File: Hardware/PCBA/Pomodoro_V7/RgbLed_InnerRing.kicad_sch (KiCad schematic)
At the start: 8 parts

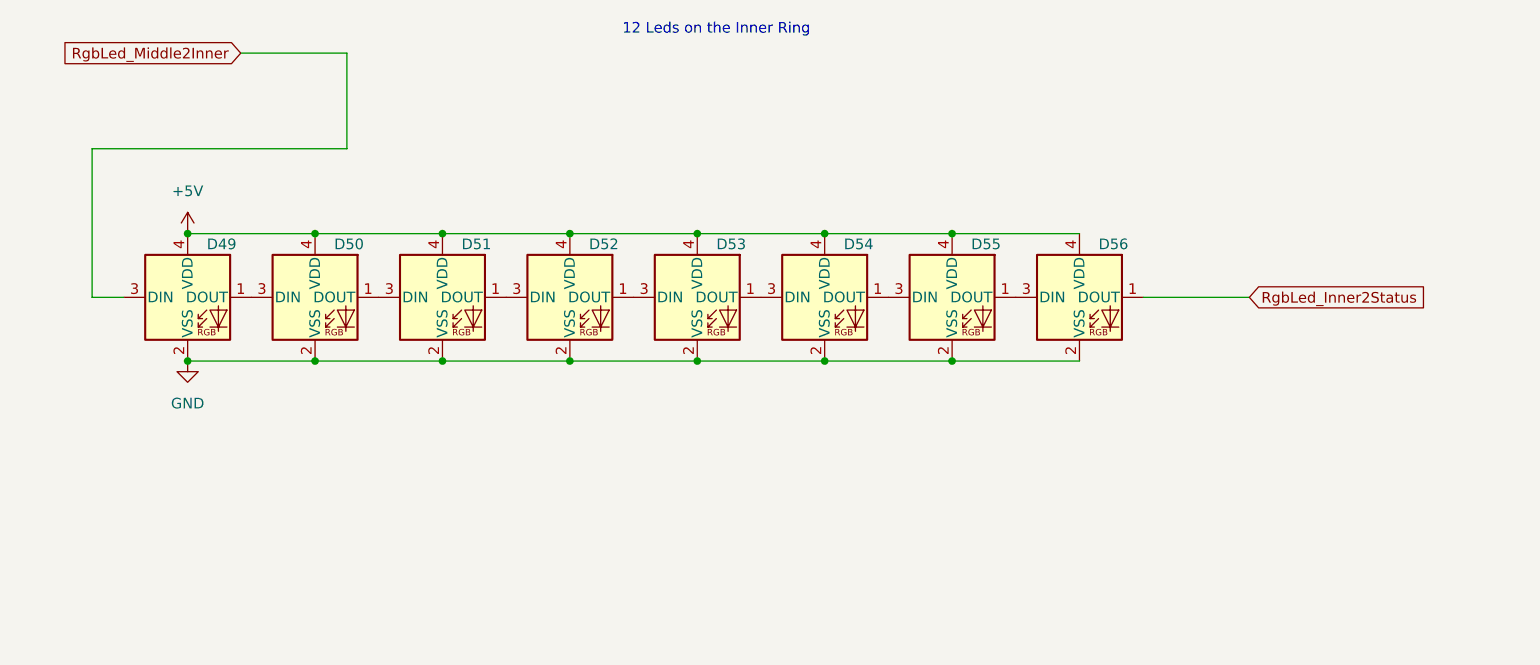
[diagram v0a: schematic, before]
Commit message: FW can now be flashed to an ESP32-S2 Target; Completed the Schematic
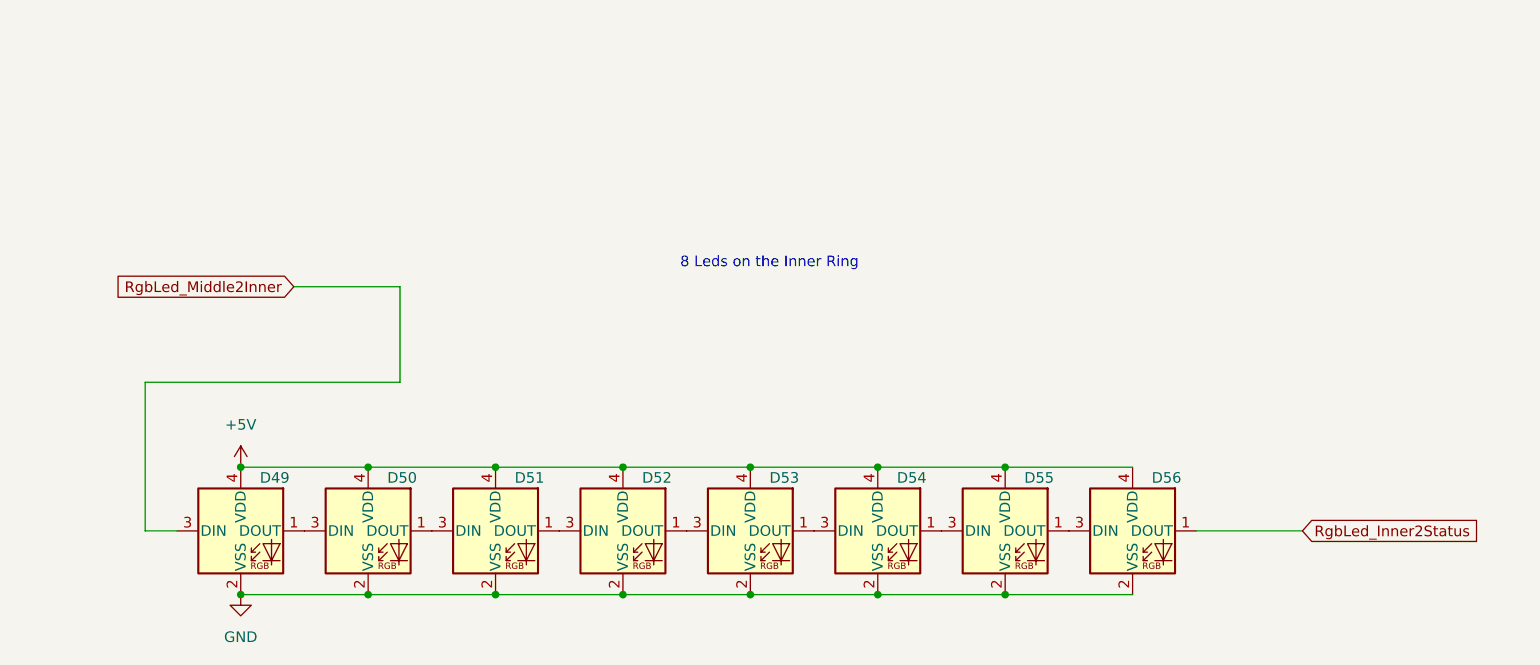
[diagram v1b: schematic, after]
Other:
- note added: "8 Leds on the Inner Ring"
- note removed: "12 Leds on the Inner Ring"
- moved on the sheet: D49, D50, D51, D52, D53, D54, D55, D56
